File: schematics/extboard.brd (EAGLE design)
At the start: 58.1 x 64.1 mm, 25 parts, among them U1 LTC1257, U2 LTC1257, X2-JACK 1503_02

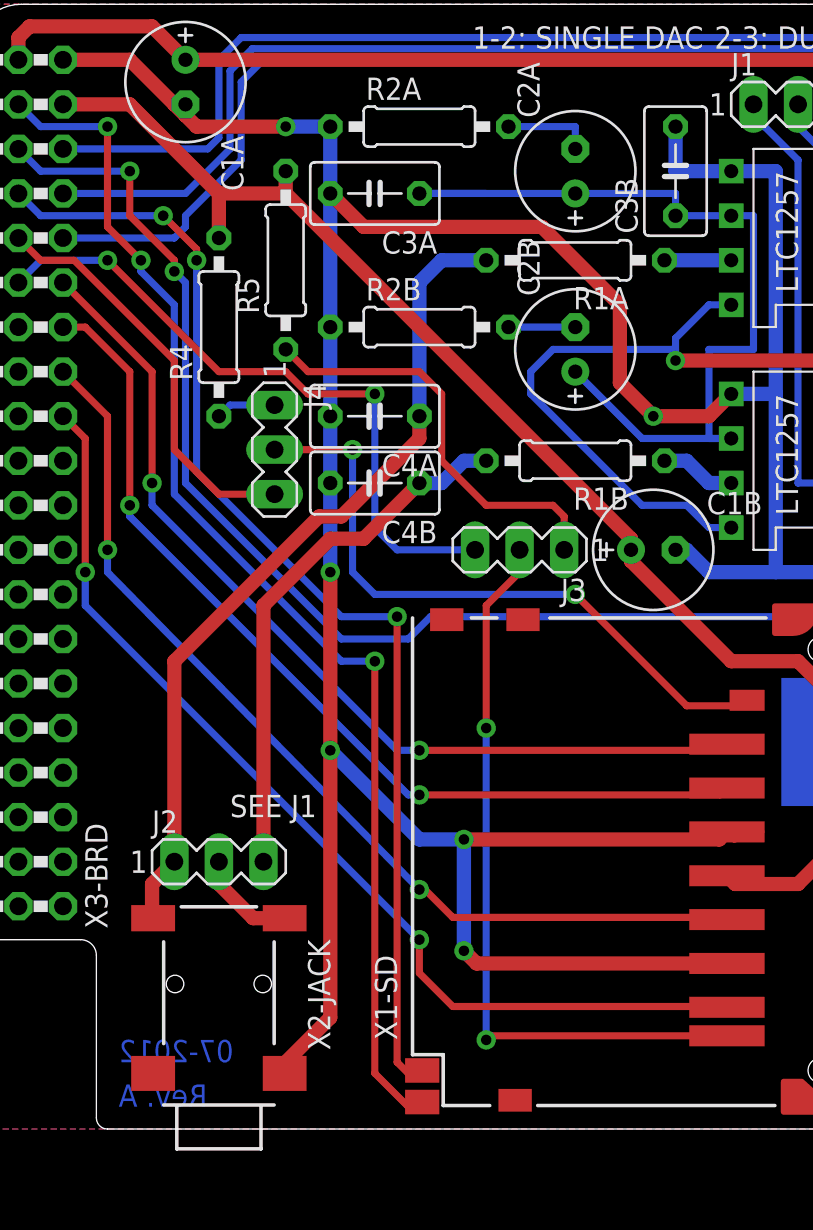
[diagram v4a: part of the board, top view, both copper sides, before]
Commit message: schematics: Elevated to Revision B (2 prototypes in production)
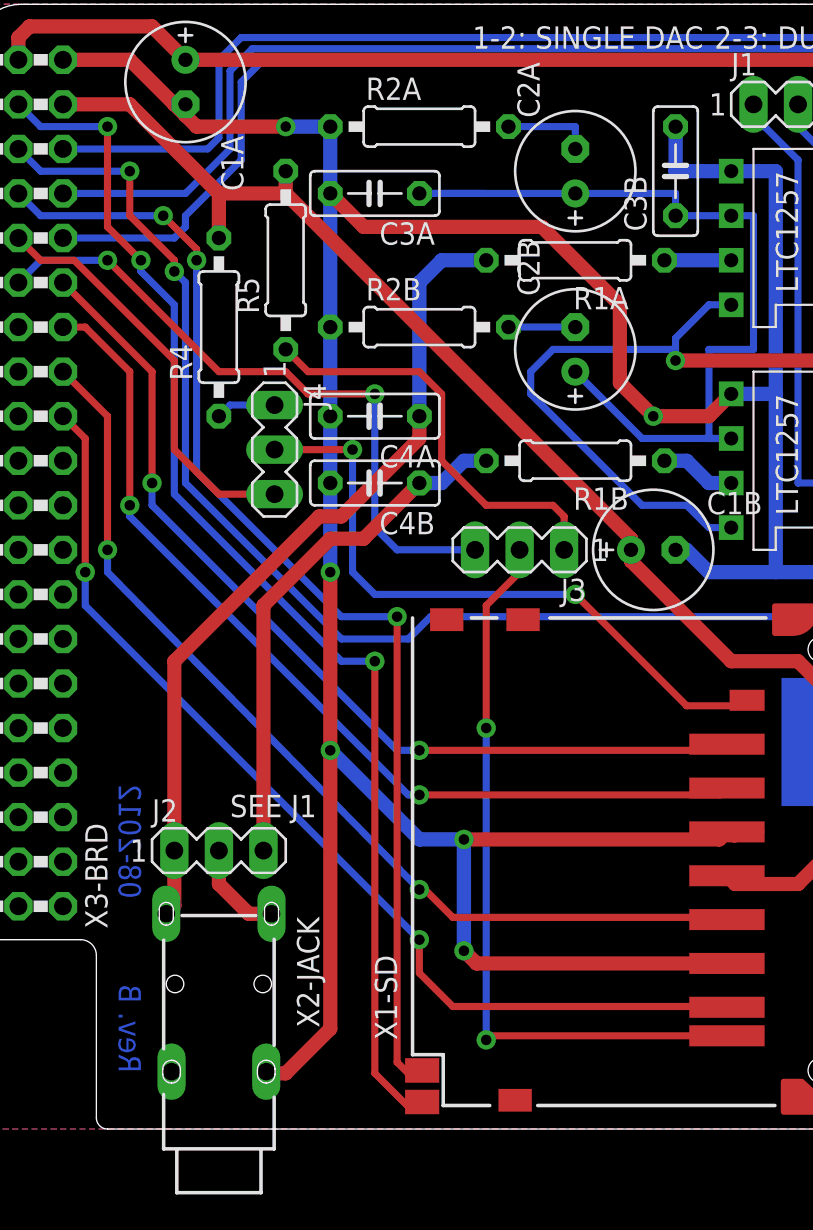
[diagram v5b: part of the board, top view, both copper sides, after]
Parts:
- C3A, C3B, C4A, C4B: device rcl:C050-035X075 -> rcl:C050-025X075
- X2-JACK: value 1503_02 -> 1503_07; device con-lumberg:1503_02 -> con-lumberg:1503_07
- moved J2 0.63 mm to (14.0, 17.1)
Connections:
- net GND: now also X2-JACK.2@1; no longer X2-JACK.2
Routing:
- net GND: track 219.3 -> 220.4 mm
- net N$21: track 30.7 -> 30.1 mm
- net N$7: track 47.7 -> 47.0 mm
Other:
- board text added: "08-2012"
- board text added: "Rev. B"
- board text removed: "07-2012"
- board text removed: "Rev. A"
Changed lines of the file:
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@@
 <wire x1="58.09" y1="64.035484375" x2="56.730484375" y2="65.395" width="0" layer="20" curve="90"/>
 <text x="50.8" y="23.1775" size="1.6764" layer="22" font="vector" ratio="20" rot="MR0" align="center">HPI</text>
-<text x="56.515" y="13.97" size="1.4224" layer="22" font="vector" ratio="15" rot="MR0">Hasso-Plattner-Instutut</text>
-<text x="56.515" y="11.43" size="1.1684" layer="22" font="vector" ratio="18" rot="MR0">für Softwaresystemtechnik GmbH</text>
-<text x="55.88" y="6.35" size="1.4224" layer="22" font="vector" ratio="15" rot="MR0">AG Systemtechnische Grundlagen</text>
-<text x="56.515" y="2.54" size="1.778" layer="22" font="vector" ratio="15" rot="MR0">SD&amp;DAC Extension Board</text>
-<text x="8.255" y="2.54" size="1.27" layer="16" font="vector" ratio="18" rot="MR0" align="bottom-right">Rev. A</text>
-<text x="8.255" y="5.08" size="1.27" layer="16" font="vector" ratio="18" rot="MR0" align="bottom-right">07-2012</text>
+<text x="56.515" y="14.605" size="1.4224" layer="22" font="vector" ratio="15" rot="MR0">Hasso-Plattner-Instutut</text>
+<text x="56.515" y="12.7" size="1.1684" layer="22" font="vector" ratio="18" rot="MR0">für Softwaresystemtechnik GmbH</text>
+<text x="56.515" y="9.525" size="1.4224" layer="22" font="vector" ratio="15" rot="MR0">AG Systemtechnische Grundlagen</text>
+<text x="56.515" y="6.985" size="1.778" layer="22" font="vector" ratio="15" rot="MR0">SD&amp;DAC Extension Board</text>
+<text x="8.255" y="9.525" size="1.27" layer="16" font="vector" ratio="18" rot="MR90" align="bottom-right">Rev. B</text>
+<text x="8.255" y="20.955" size="1.27" layer="16" font="vector" ratio="18" rot="MR90" align="bottom-right">08-2012</text>
 <text x="42.2275" y="62.865" size="1.27" layer="21" font="vector" ratio="18">2-3: DUAL DAC</text>
 <text x="41.5925" y="62.865" size="1.27" layer="21" font="vector" ratio="18" align="bottom-right">1-2: SINGLE DAC</text>
@@
 <element name="R5" library="rcl" package="0207/10" value="10k" x="17.78" y="50.8" rot="R90"/>
 <element name="R3A" library="rcl" package="0207/10" value="10k" x="53.34" y="52.07" rot="R270"/>
-<element name="C3A" library="rcl" package="C050-035X075" value="0u1" x="22.86" y="54.61" rot="R180"/>
-<element name="C4A" library="rcl" package="C050-035X075" value="0u1" x="22.86" y="41.91" rot="R180"/>
+<element name="C3A" library="rcl" package="C050-025X075" value="0u1" x="22.86" y="54.61" rot="R180"/>
+<element name="C4A" library="rcl" package="C050-025X075" value="0u1" x="22.86" y="41.91" rot="R180"/>
 <element name="C1A" library="rcl" package="E2,5-7" value="2u2" x="12.065" y="60.96" rot="R270"/>
 <element name="C2A" library="rcl" package="E2,5-7" value="2u2" x="34.29" y="55.88" rot="R90"/>
@@
 <element name="R1B" library="rcl" package="0207/10" value="250" x="34.29" y="39.37" rot="R180"/>
 <element name="R2B" library="rcl" package="0207/10" value="10" x="25.4" y="46.99"/>
-<element name="C3B" library="rcl" package="C050-035X075" value="0u1" x="40.005" y="55.88" rot="R90"/>
-<element name="C4B" library="rcl" package="C050-035X075" value="0u1" x="22.86" y="38.1" rot="R180"/>
+<element name="C3B" library="rcl" package="C050-025X075" value="0u1" x="40.005" y="55.88" rot="R90"/>
+<element name="C4B" library="rcl" package="C050-025X075" value="0u1" x="22.86" y="38.1" rot="R180"/>
 <element name="C2B" library="rcl" package="E2,5-7" value="2u2" x="34.29" y="45.72" rot="R90"/>
 <element name="J1" library="con-lstb" package="MA03-1" value="" x="46.99" y="59.69">
@@
 <attribute name="OC_FARNELL" value="unknown" x="46.99" y="59.69" size="1.778" layer="27" display="off"/>
 </element>
-<element name="J2" library="con-lstb" package="MA03-1" value="" x="13.97" y="16.51">
-<attribute name="OC_NEWARK" value="unknown" x="13.97" y="16.51" size="1.778" layer="27" display="off"/>
-<attribute name="MPN" value="" x="13.97" y="16.51" size="1.778" layer="27" display="off"/>
-<attribute name="MF" value="" x="13.97" y="16.51" size="1.778" layer="27" display="off"/>
-<attribute name="OC_FARNELL" value="unknown" x="13.97" y="16.51" size="1.778" layer="27" display="off"/>
+<element name="J2" library="con-lstb" package="MA03-1" value="" x="13.97" y="17.145">
+<attribute name="OC_NEWARK" value="unknown" x="13.97" y="17.145" size="1.778" layer="27" display="off"/>
+<attribute name="MPN" value="" x="13.97" y="17.145" size="1.778" layer="27" display="off"/>
+<attribute name="MF" value="" x="13.97" y="17.145" size="1.778" layer="27" display="off"/>
+<attribute name="OC_FARNELL" value="unknown" x="13.97" y="17.145" size="1.778" layer="27" display="off"/>
 </element>
-<element name="X2-JACK" library="con-lumberg" package="1503_02" value="1503_02" x="13.97" y="2.54" rot="R180">
+<element name="X2-JACK" library="con-lumberg" package="1503_07" value="1503_07" x="13.97" y="2.54" rot="R180">
 <attribute name="OC_NEWARK" value="unknown" x="13.97" y="2.54" size="1.778" layer="27" rot="R180" display="off"/>
 <attribute name="MPN" value="" x="13.97" y="2.54" size="1.778" layer="27" rot="R180" display="off"/>
 <attribute name="MF" value="" x="13.97" y="2.54" size="1.778" layer="27" rot="R180" display="off"/>
-<attribute name="OC_FARNELL" value="1216979" x="13.97" y="2.54" size="1.778" layer="27" rot="R180" display="off"/>
+<attribute name="OC_FARNELL" value="unknown" x="13.97" y="2.54" size="1.778" layer="27" rot="R180" display="off"/>
 </element>
 <element name="X1-SD" library="farnell-sd" package="SDBMF-009XXBXX2" value="" x="48.26" y="16.51" rot="R90"/>
@@
 <contactref element="R3A" pad="2"/>
 <wire x1="53.34" y1="46.99" x2="55.88" y2="46.99" width="0.8128" layer="16"/>
-<contactref element="X2-JACK" pad="2"/>
-<wire x1="20.32" y1="7.62" x2="20.32" y2="22.86" width="0.8128" layer="1"/>
+<contactref element="X2-JACK" pad="2@1"/>
+<wire x1="20.32" y1="6.985" x2="20.32" y2="22.86" width="0.8128" layer="1"/>
 <via x="20.32" y="33.02" extent="1-16" drill="0.6"/>
 <polygon width="0.4064" layer="16">
@@
 <wire x1="25.4" y1="17.78" x2="20.32" y2="22.86" width="0.8128" layer="16"/>
 <via x="20.32" y="22.86" extent="1-16" drill="0.6"/>
-<wire x1="20.32" y1="7.62" x2="17.78" y2="5.08" width="0.8128" layer="1"/>
 <wire x1="40.005" y1="34.29" x2="40.64" y2="34.29" width="0.8128" layer="16"/>
 <wire x1="40.64" y1="34.29" x2="41.91" y2="33.02" width="0.8128" layer="16"/>
@@
 <wire x1="11.43" y1="59.69" x2="12.065" y2="59.055" width="0.8128" layer="1"/>
 <wire x1="12.065" y1="59.69" x2="11.43" y2="59.69" width="0.8128" layer="1"/>
-<wire x1="17.78" y1="5.08" x2="17.78" y2="4.5" width="0.8128" layer="1"/>
-<wire x1="17.78" y1="4.5" x2="17.72" y2="4.44" width="0.8128" layer="1"/>
+<wire x1="20.32" y1="6.985" x2="17.78" y2="4.445" width="0.8128" layer="1"/>
+<wire x1="17.78" y1="4.445" x2="16.765" y2="4.445" width="0.8128" layer="1"/>
+<wire x1="16.765" y1="4.445" x2="16.67" y2="4.54" width="0.8128" layer="1"/>
 </signal>
 <signal name="N$2">
@@
 <contactref element="J2" pad="1"/>
 <contactref element="X2-JACK" pad="3"/>
-<wire x1="11.43" y1="16.51" x2="11.43" y2="27.94" width="0.8128" layer="1"/>
+<wire x1="11.43" y1="17.145" x2="11.43" y2="27.94" width="0.8128" layer="1"/>
 <wire x1="11.43" y1="27.94" x2="19.685" y2="36.195" width="0.8128" layer="1"/>
 <wire x1="19.685" y1="36.195" x2="20.955" y2="36.195" width="0.8128" layer="1"/>
@@
 <wire x1="25.4" y1="49.53" x2="26.67" y2="50.8" width="0.8128" layer="16"/>
 <wire x1="26.67" y1="50.8" x2="29.21" y2="50.8" width="0.8128" layer="16"/>
-<wire x1="11.43" y1="16.51" x2="10.16" y2="15.24" width="0.8128" layer="1"/>
-<wire x1="10.16" y1="15.24" x2="10.16" y2="13.35" width="0.8128" layer="1"/>
-<wire x1="10.16" y1="13.35" x2="10.22" y2="13.29" width="0.8128" layer="1"/>
+<wire x1="11.43" y1="17.145" x2="11.43" y2="14" width="0.8128" layer="1"/>
+<wire x1="11.43" y1="14" x2="10.97" y2="13.54" width="0.8128" layer="1"/>
 </signal>
 <signal name="N$8">
@@
 <contactref element="R1B" pad="2"/>
 <contactref element="J2" pad="3"/>
-<wire x1="16.51" y1="16.51" x2="16.51" y2="31.115" width="0.8128" layer="1"/>
+<wire x1="16.51" y1="17.145" x2="16.51" y2="31.115" width="0.8128" layer="1"/>
 <wire x1="16.51" y1="31.115" x2="20.32" y2="34.925" width="0.8128" layer="1"/>
 <wire x1="20.32" y1="34.925" x2="22.225" y2="34.925" width="0.8128" layer="1"/>
@@
 <contactref element="J2" pad="2"/>
 <contactref element="X2-JACK" pad="1"/>
-<wire x1="17.72" y1="13.29" x2="15.92" y2="13.29" width="0.8128" layer="1"/>
-<wire x1="15.92" y1="13.29" x2="13.97" y2="15.24" width="0.8128" layer="1"/>
-<wire x1="13.97" y1="15.24" x2="13.97" y2="16.51" width="0.8128" layer="1"/>
+<wire x1="16.97" y1="13.54" x2="15.67" y2="13.54" width="0.8128" layer="1"/>
+<wire x1="15.67" y1="13.54" x2="13.97" y2="15.24" width="0.8128" layer="1"/>
+<wire x1="13.97" y1="15.24" x2="13.97" y2="17.145" width="0.8128" layer="1"/>
 </signal>
 <signal name="N$20">
